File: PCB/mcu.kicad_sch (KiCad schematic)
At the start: 36 parts

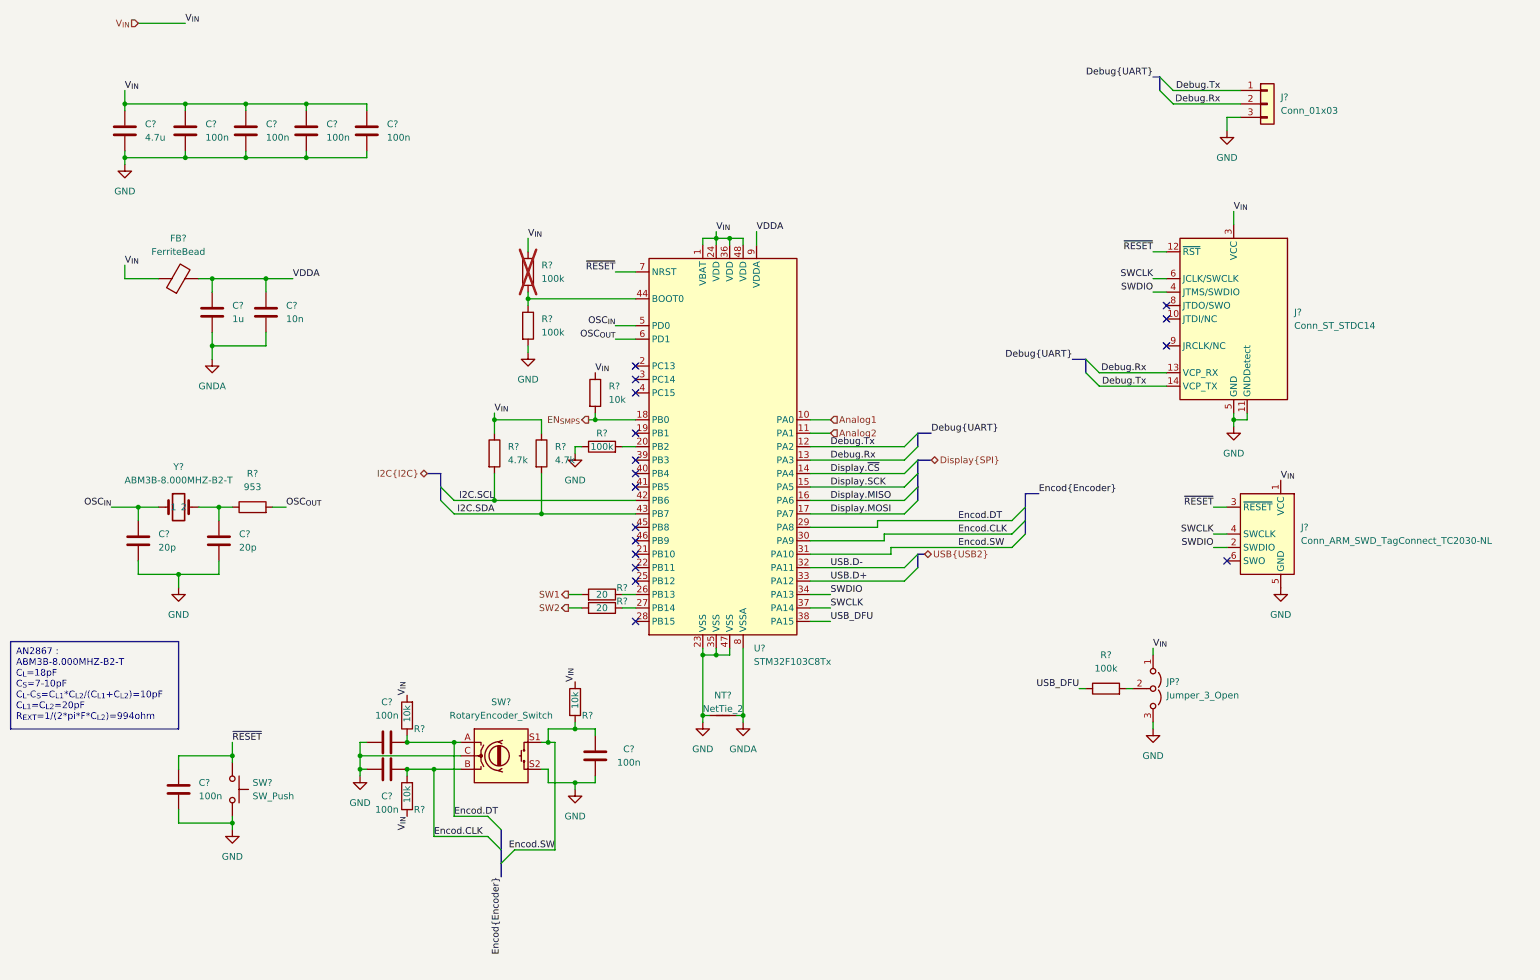
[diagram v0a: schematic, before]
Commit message: done with sch before ERC and footprints
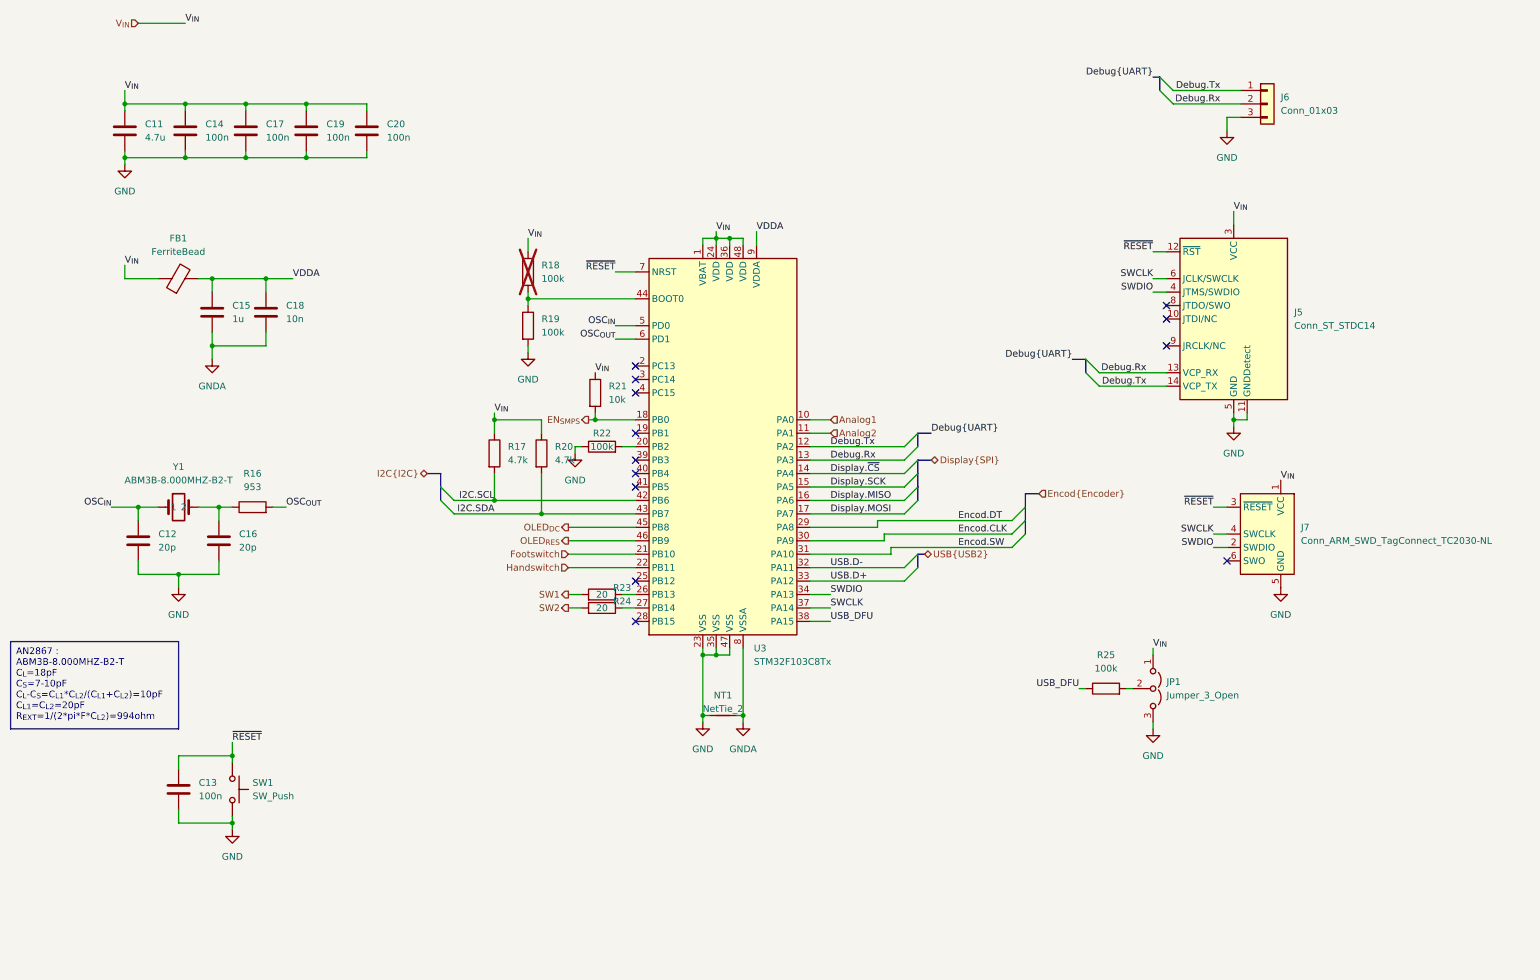
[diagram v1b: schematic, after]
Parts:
- removed C? (x3): 100n, symbol Device:C
- removed R? (x3): 10k, symbol Device:R
- removed SW?: RotaryEncoder_Switch, symbol Device:RotaryEncoder_Switch
- gave numbers to parts that had none: 29
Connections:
- net Footswitch: now reaches U3.21 (PB10)
- net Handswitch: now reaches U3.22 (PB11)
- net OLED_{DC}: now reaches U3.45 (PB8)
- net OLED_{RES}: now reaches U3.46 (PB9)
- no-connect marks 17 -> 13

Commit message: begin BOM
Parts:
- C11: footprint (none) -> Capacitor_SMD:C_0805_2012Metric; MPN (none) -> GRM219R6YA475KA73D; Manufacturer (none) -> Murata
- C12, C16: footprint (none) -> Capacitor_SMD:C_0603_1608Metric; MPN (none) -> C0603C200J5HACTU; Manufacturer (none) -> Kemet
- C13, C14, C17, C19, C20: footprint (none) -> Capacitor_SMD:C_0603_1608Metric; MPN (none) -> CGA3E2X7R1H104M080AA; Manufacturer (none) -> TDK
- C15: footprint (none) -> Capacitor_SMD:C_0603_1608Metric; MPN (none) -> CGA3E1X7R1V105K080AC; Manufacturer (none) -> TDK
- C18: footprint (none) -> Capacitor_SMD:C_0603_1608Metric; MPN (none) -> GCM188R71H103KA37J; Manufacturer (none) -> Murata

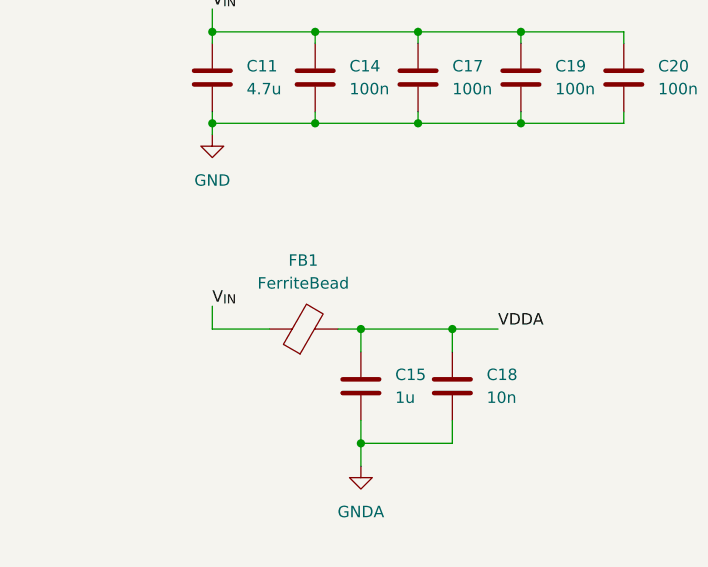
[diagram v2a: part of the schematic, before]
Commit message: Resistors ok in BOM
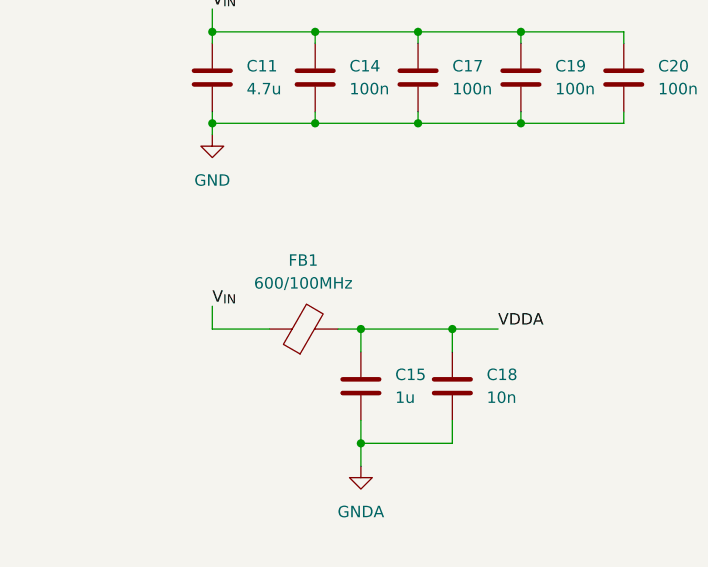
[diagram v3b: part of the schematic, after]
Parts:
- FB1: value FerriteBead -> 600/100MHz; footprint (none) -> Resistor_SMD:R_0603_1608Metric; MPN (none) -> 742792651; Manufacturer (none) -> Wurth Elektronik
- R16: footprint (none) -> Resistor_SMD:R_0603_1608Metric; MPN (none) -> ERJ-3EKF9530V; Manufacturer (none) -> Panasonic
- R17, R20: footprint (none) -> Resistor_SMD:R_0603_1608Metric; MPN (none) -> ERJ-3EKF4701V; Manufacturer (none) -> Panasonic
- R18, R19, R22, R25: footprint (none) -> Resistor_SMD:R_0603_1608Metric; MPN (none) -> ERJ-3EKF1003V; Manufacturer (none) -> Panasonic
- R21: footprint (none) -> Resistor_SMD:R_0603_1608Metric; MPN (none) -> ERJ-3EKF1002V; Manufacturer (none) -> Panasonic
- R23, R24: footprint (none) -> Resistor_SMD:R_0603_1608Metric; MPN (none) -> ERJ-3EKF20R0V; Manufacturer (none) -> Panasonic
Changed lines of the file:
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@@
       (effects (font (size 1.27 1.27)))
     )
-    (property "Footprint" "" (at 124.46 102.108 90)
+    (property "Footprint" "Resistor_SMD:R_0603_1608Metric" (at 124.46 102.108 90)
       (effects (font (size 1.27 1.27)) hide)
     )
@@
       (effects (font (size 1.27 1.27)) hide)
     )
-    (property "MPN" "" (at 124.46 100.33 0)
-      (effects (font (size 1.27 1.27)) hide)
-    )
-    (property "Manufacturer" "" (at 124.46 100.33 0)
+    (property "MPN" "ERJ-3EKF1003V" (at 124.46 100.33 0)
+      (effects (font (size 1.27 1.27)) hide)
+    )
+    (property "Manufacturer" "Panasonic" (at 124.46 100.33 0)
       (effects (font (size 1.27 1.27)) hide)
     )
@@
       (effects (font (size 1.27 1.27)))
     )
-    (property "Footprint" "" (at 58.42 113.538 90)
+    (property "Footprint" "Resistor_SMD:R_0603_1608Metric" (at 58.42 113.538 90)
       (effects (font (size 1.27 1.27)) hide)
     )
@@
       (effects (font (size 1.27 1.27)) hide)
     )
-    (property "MPN" "" (at 58.42 111.76 0)
-      (effects (font (size 1.27 1.27)) hide)
-    )
-    (property "Manufacturer" "" (at 58.42 111.76 0)
+    (property "MPN" "ERJ-3EKF9530V" (at 58.42 111.76 0)
+      (effects (font (size 1.27 1.27)) hide)
+    )
+    (property "Manufacturer" "Panasonic" (at 58.42 111.76 0)
       (effects (font (size 1.27 1.27)) hide)
     )
@@
       (effects (font (size 1.27 1.27)))
     )
-    (property "Footprint" "" (at 219.71 147.828 90)
+    (property "Footprint" "Resistor_SMD:R_0603_1608Metric" (at 219.71 147.828 90)
       (effects (font (size 1.27 1.27)) hide)
     )
@@
       (effects (font (size 1.27 1.27)) hide)
     )
-    (property "MPN" "" (at 219.71 146.05 0)
-      (effects (font (size 1.27 1.27)) hide)
-    )
-    (property "Manufacturer" "" (at 219.71 146.05 0)
+    (property "MPN" "ERJ-3EKF1003V" (at 219.71 146.05 0)
+      (effects (font (size 1.27 1.27)) hide)
+    )
+    (property "Manufacturer" "Panasonic" (at 219.71 146.05 0)
       (effects (font (size 1.27 1.27)) hide)
     )
@@
       (effects (font (size 1.27 1.27)) (justify left))
     )
-    (property "Footprint" "" (at 121.412 90.17 90)
+    (property "Footprint" "Resistor_SMD:R_0603_1608Metric" (at 121.412 90.17 90)
       (effects (font (size 1.27 1.27)) hide)
     )
@@
       (effects (font (size 1.27 1.27)) hide)
     )
-    (property "MPN" "" (at 123.19 90.17 0)
-      (effects (font (size 1.27 1.27)) hide)
-    )
-    (property "Manufacturer" "" (at 123.19 90.17 0)
+    (property "MPN" "ERJ-3EKF1002V" (at 123.19 90.17 0)
+      (effects (font (size 1.27 1.27)) hide)
+    )
+    (property "Manufacturer" "Panasonic" (at 123.19 90.17 0)
       (effects (font (size 1.27 1.27)) hide)
     )
@@
       (effects (font (size 1.27 1.27)) (justify left))
     )
-    (property "Footprint" "" (at 108.712 67.31 90)
+    (property "Footprint" "Resistor_SMD:R_0603_1608Metric" (at 108.712 67.31 90)
       (effects (font (size 1.27 1.27)) hide)
     )
@@
       (effects (font (size 1.27 1.27)) hide)
     )
-    (property "MPN" "" (at 110.49 67.31 0)
-      (effects (font (size 1.27 1.27)) hide)
-    )
-    (property "Manufacturer" "" (at 110.49 67.31 0)
+    (property "MPN" "ERJ-3EKF1003V" (at 110.49 67.31 0)
+      (effects (font (size 1.27 1.27)) hide)
+    )
+    (property "Manufacturer" "Panasonic" (at 110.49 67.31 0)
       (effects (font (size 1.27 1.27)) hide)
     )
@@
       (effects (font (size 1.27 1.27)) (justify left))
     )
-    (property "Footprint" "" (at 102.362 101.6 90)
+    (property "Footprint" "Resistor_SMD:R_0603_1608Metric" (at 102.362 101.6 90)
       (effects (font (size 1.27 1.27)) hide)
     )
@@
       (effects (font (size 1.27 1.27)) hide)
     )
-    (property "MPN" "" (at 104.14 101.6 0)
-      (effects (font (size 1.27 1.27)) hide)
-    )
-    (property "Manufacturer" "" (at 104.14 101.6 0)
+    (property "MPN" "ERJ-3EKF4701V" (at 104.14 101.6 0)
+      (effects (font (size 1.27 1.27)) hide)
+    )
+    (property "Manufacturer" "Panasonic" (at 104.14 101.6 0)
       (effects (font (size 1.27 1.27)) hide)
     )
@@
       (effects (font (size 1.27 1.27)) (justify left))
     )
-    (property "Footprint" "" (at 108.712 77.47 90)
+    (property "Footprint" "Resistor_SMD:R_0603_1608Metric" (at 108.712 77.47 90)
       (effects (font (size 1.27 1.27)) hide)
     )
@@
       (effects (font (size 1.27 1.27)) hide)
     )
-    (property "MPN" "" (at 110.49 77.47 0)
-      (effects (font (size 1.27 1.27)) hide)
-    )
-    (property "Manufacturer" "" (at 110.49 77.47 0)
+    (property "MPN" "ERJ-3EKF1003V" (at 110.49 77.47 0)
+      (effects (font (size 1.27 1.27)) hide)
+    )
+    (property "Manufacturer" "Panasonic" (at 110.49 77.47 0)
       (effects (font (size 1.27 1.27)) hide)
     )
@@
       (effects (font (size 1.27 1.27)))
     )
-    (property "Value" "FerriteBead" (at 44.3992 63.5 90)
-      (effects (font (size 1.27 1.27)))
-    )
-    (property "Footprint" "" (at 44.45 70.358 90)
+    (property "Value" "600/100MHz" (at 44.3992 63.5 90)
+      (effects (font (size 1.27 1.27)))
+    )
+    (property "Footprint" "Resistor_SMD:R_0603_1608Metric" (at 44.45 70.358 90)
       (effects (font (size 1.27 1.27)) hide)
     )
@@
       (effects (font (size 1.27 1.27)) hide)
     )
-    (property "MPN" "" (at 44.45 68.58 0)
-      (effects (font (size 1.27 1.27)) hide)
-    )
-    (property "Manufacturer" "" (at 44.45 68.58 0)
+    (property "MPN" "742792651" (at 44.45 68.58 0)
+      (effects (font (size 1.27 1.27)) hide)
+    )
+    (property "Manufacturer" "Wurth Elektronik" (at 44.45 68.58 0)
       (effects (font (size 1.27 1.27)) hide)
     )
@@
       (effects (font (size 1.27 1.27)) (justify left))
     )
-    (property "Footprint" "" (at 111.252 101.6 90)
+    (property "Footprint" "Resistor_SMD:R_0603_1608Metric" (at 111.252 101.6 90)
       (effects (font (size 1.27 1.27)) hide)
     )
@@
       (effects (font (size 1.27 1.27)) hide)
     )
-    (property "MPN" "" (at 113.03 101.6 0)
-      (effects (font (size 1.27 1.27)) hide)
-    )
-    (property "Manufacturer" "" (at 113.03 101.6 0)
+    (property "MPN" "ERJ-3EKF4701V" (at 113.03 101.6 0)
+      (effects (font (size 1.27 1.27)) hide)
+    )
+    (property "Manufacturer" "Panasonic" (at 113.03 101.6 0)
       (effects (font (size 1.27 1.27)) hide)
     )
@@
       (effects (font (size 1.27 1.27)))
     )
-    (property "Footprint" "" (at 124.46 132.588 90)
+    (property "Footprint" "Resistor_SMD:R_0603_1608Metric" (at 124.46 132.588 90)
       (effects (font (size 1.27 1.27)) hide)
     )
@@
       (effects (font (size 1.27 1.27)) hide)
     )
-    (property "MPN" "" (at 124.46 130.81 0)
-      (effects (font (size 1.27 1.27)) hide)
-    )
-    (property "Manufacturer" "" (at 124.46 130.81 0)
+    (property "MPN" "ERJ-3EKF20R0V" (at 124.46 130.81 0)
+      (effects (font (size 1.27 1.27)) hide)
+    )
+    (property "Manufacturer" "Panasonic" (at 124.46 130.81 0)
       (effects (font (size 1.27 1.27)) hide)
     )
@@
       (effects (font (size 1.27 1.27)))
     )
-    (property "Footprint" "" (at 124.46 130.048 90)
+    (property "Footprint" "Resistor_SMD:R_0603_1608Metric" (at 124.46 130.048 90)
       (effects (font (size 1.27 1.27)) hide)
     )
@@
       (effects (font (size 1.27 1.27)) hide)
     )
-    (property "MPN" "" (at 124.46 128.27 0)
-      (effects (font (size 1.27 1.27)) hide)
-    )
-    (property "Manufacturer" "" (at 124.46 128.27 0)
-      (effects (font (size 1.27 1.27)) hide)
-    )
+    (property "MPN" "ERJ-3EKF20R0V" (at 124.46 128.27 0)
+      (effects (font (size 1.27 1.27)) hide)
+    )
+    (property "Manufacturer" "Panasonic" (at 124.46 128.27 0)
+      (effects (font (size 1.27 1.27)) hide)
+    )

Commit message: bom almost finished
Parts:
- U3: MPN (none) -> STM32F103C8T6; Manufacturer (none) -> STMicroelectronics
- Y1: MPN (none) -> ABM3B-8.000MHZ-B2-T; Manufacturer (none) -> Abracon
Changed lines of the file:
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@@
       (effects (font (size 1.27 1.27)) hide)
     )
-    (property "MPN" "" (at 44.45 111.76 0)
-      (effects (font (size 1.27 1.27)) hide)
-    )
-    (property "Manufacturer" "" (at 44.45 111.76 0)
+    (property "MPN" "ABM3B-8.000MHZ-B2-T" (at 44.45 111.76 0)
+      (effects (font (size 1.27 1.27)) hide)
+    )
+    (property "Manufacturer" "Abracon" (at 44.45 111.76 0)
       (effects (font (size 1.27 1.27)) hide)
     )
@@
       (effects (font (size 1.27 1.27)) hide)
     )
-    (property "MPN" "" (at 148.59 100.33 0)
-      (effects (font (size 1.27 1.27)) hide)
-    )
-    (property "Manufacturer" "" (at 148.59 100.33 0)
-      (effects (font (size 1.27 1.27)) hide)
-    )
+    (property "MPN" "STM32F103C8T6" (at 148.59 100.33 0)
+      (effects (font (size 1.27 1.27)) hide)
+    )
+    (property "Manufacturer" "STMicroelectronics " (at 148.59 100.33 0)
+      (effects (font (size 1.27 1.27)) hide)
+    )
